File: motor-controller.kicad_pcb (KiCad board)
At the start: 2 copper layers, 40 x 40 mm, 34 parts, among them J1 GH1.25, J2 GH1.25, J3 GH1.25, J4 SM03B-PASS, U1 SSP7903P33PR, U2 AS5600, U3 SS6343M, U4 STM32F031C6T6, Y1 YSX530GA 8MHz

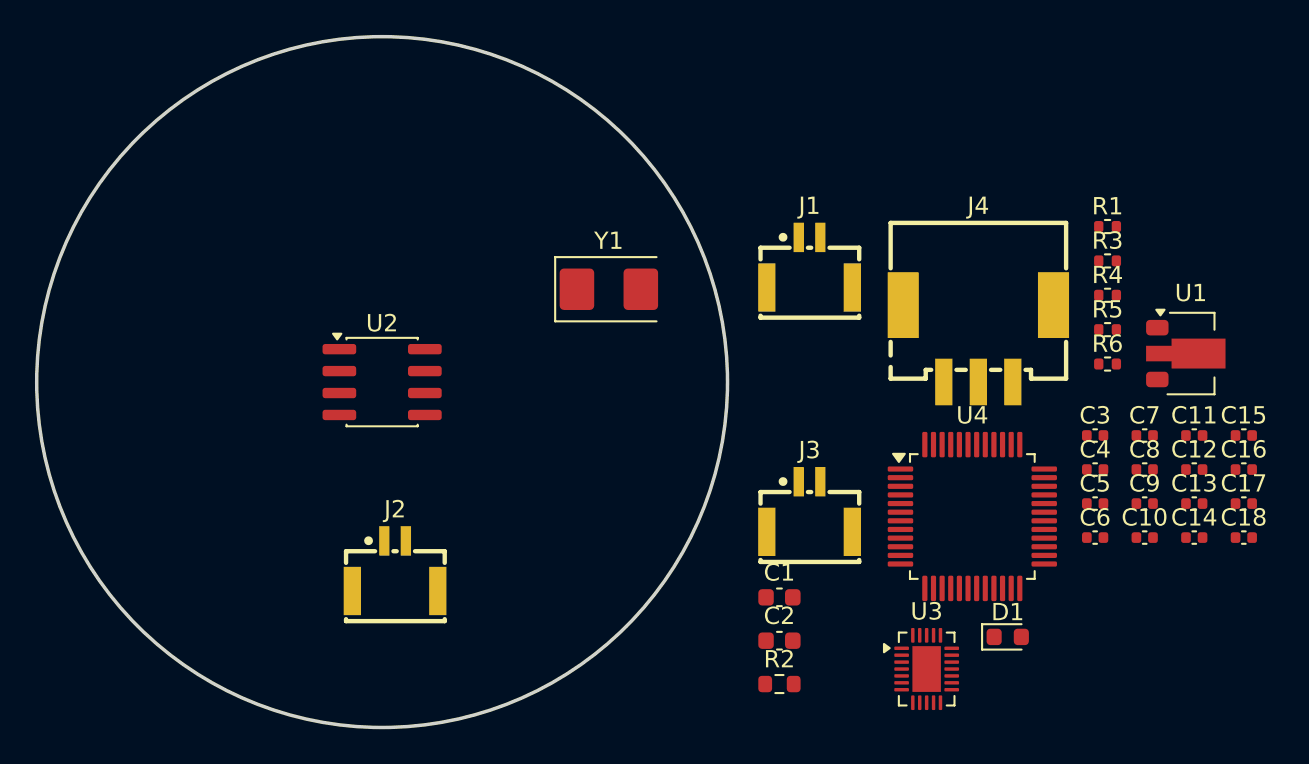
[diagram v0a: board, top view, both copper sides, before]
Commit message: 完成PCB布局
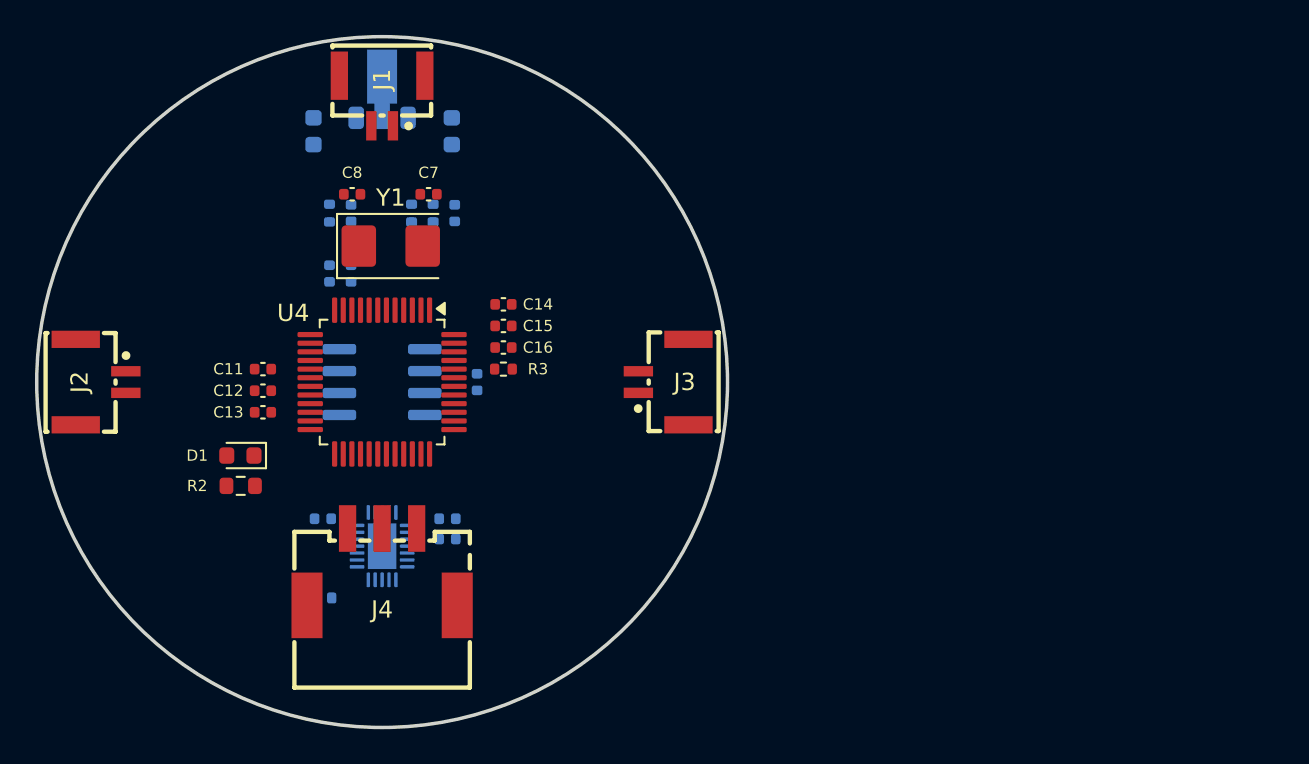
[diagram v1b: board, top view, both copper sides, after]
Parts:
- C1, C10, C17, C18, C2, C3, C4, C5, C6, C9, R1, R4, R5, R6, U1, U2, U3: moved to B.Cu
- moved C17 54.6 mm to (147.0, 91.7), turned to 90 degrees
- moved C13 54.2 mm to (143.1, 99.8)
- moved C12 54.1 mm to (143.1, 98.5)
- moved C11 54.1 mm to (143.1, 97.2)
- moved C18 53.9 mm to (148.2, 91.7), turned to 90 degrees
- moved R1 50.3 mm to (146.6, 110.5), turned to 180 degrees
- moved U1 49.4 mm to (150.0, 80.8), turned to 90 degrees
- moved C9 48.9 mm to (148.2, 88.2), turned to 90 degrees
- moved C8 48.6 mm to (148.3, 87.1), turned to 180 degrees
- moved D1 45.7 mm to (141.8, 102.3), turned to 180 degrees
- moved R4 45.3 mm to (147.0, 88.2), turned to -90 degrees
- moved C6 44.7 mm to (146.6, 105.9), turned to 180 degrees
- moved C10 44.1 mm to (154.2, 88.2), turned to -90 degrees
- moved C7 43.8 mm to (152.7, 87.1)
- moved C16 43.4 mm to (157.0, 96.0)
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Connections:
- J1 pad 1: 12V -> GND
- J1 pad 2: GND -> 12V
- J4 pad 1: /C -> /A
- J4 pad 3: /A -> /C

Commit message: 重新布局并完成布线，添加STM项目定义文件
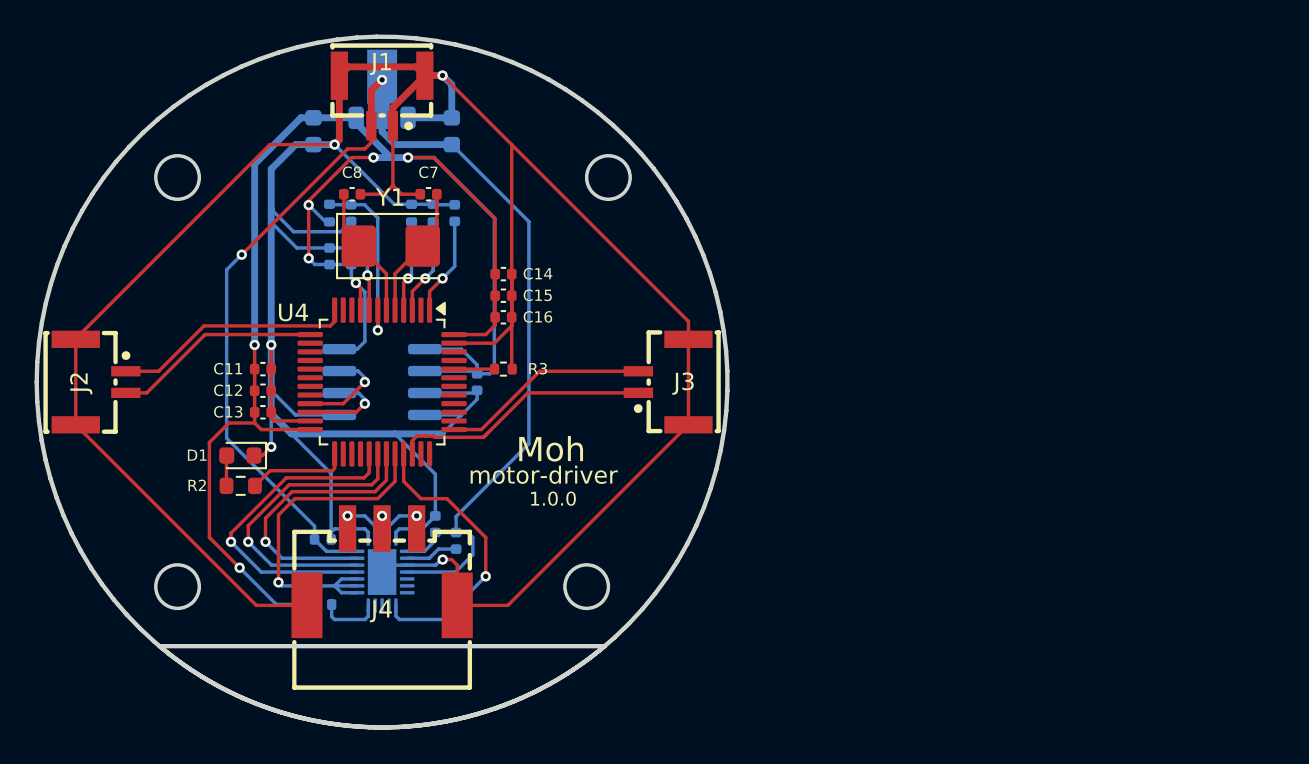
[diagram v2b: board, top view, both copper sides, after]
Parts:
- moved C14 1.75 mm to (157.0, 91.8)
- moved C15 1.75 mm to (157.0, 93.0)
- moved C16 1.75 mm to (157.0, 94.2)
- moved U3 1.50 mm to (150.0, 109.0)
- moved C6 1.19 mm to (146.6, 107.1), turned to 0 degrees
- moved C17 1.00 mm to (147.0, 90.7)
- moved C18 1.00 mm to (148.2, 90.7)
- moved C5 0.77 mm to (153.1, 106.2), turned to 90 degrees
- moved C4 0.51 mm to (154.3, 107.2), turned to 90 degrees
- moved R1 0.38 mm to (146.6, 110.9)
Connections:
- J1 pad 3: (no net) -> GND
- J1 pad 4: (no net) -> GND
- J2 pad 3: (no net) -> GND
- J2 pad 4: (no net) -> GND
- J3 pad 3: (no net) -> GND
- J3 pad 4: (no net) -> GND
- J4 pad 4: (no net) -> GND
- J4 pad 5: (no net) -> GND
- U4 pad 12: unconnected-(U4-PA2-Pad12) -> /Tx
- U4 pad 26: /FAULT -> unconnected-(U4-PB13-Pad26)
- U4 pad 33: unconnected-(U4-PA12-Pad33) -> /FAULT
- U4 pad 42: /Tx -> unconnected-(U4-PB6-Pad42)
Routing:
- net GND: track 0.00 -> 233.7 mm, vias 0 -> 6
- net 3.3V: track 0.00 -> 105.9 mm, vias 0 -> 7
- net 12V: track 0.00 -> 76.9 mm, vias 0 -> 2
- net /EN: track 0.00 -> 20.6 mm, vias 0 -> 1
- net /PWMA: track 0.00 -> 19.1 mm, vias 0 -> 1
- net /PWMB: track 0.00 -> 17.9 mm, vias 0 -> 1
- net /FAULT: track 0.00 -> 16.9 mm, vias 0 -> 1
- net /PWMC: track 0.00 -> 16.5 mm, vias 0 -> 1
- net /SWDIO: track 0.00 -> 15.5 mm
- net /Tx: track 0.00 -> 13.9 mm
- net /SWCLK: track 0.00 -> 12.1 mm
- net /Rx: track 0.00 -> 12.1 mm
- net /RST: track 0.00 -> 10.8 mm, vias 0 -> 1
- net /X1: track 0.00 -> 7.73 mm
- net /X0: track 0.00 -> 7.71 mm
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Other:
- outline, holes or cut-outs redrawn
- board text added: "1.0.0"
- board text added: "Moh"
- board text added: "motor-driver"

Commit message: 将板框从圆环多边形修改为圆弧和直线组合，避免gerber文件混淆
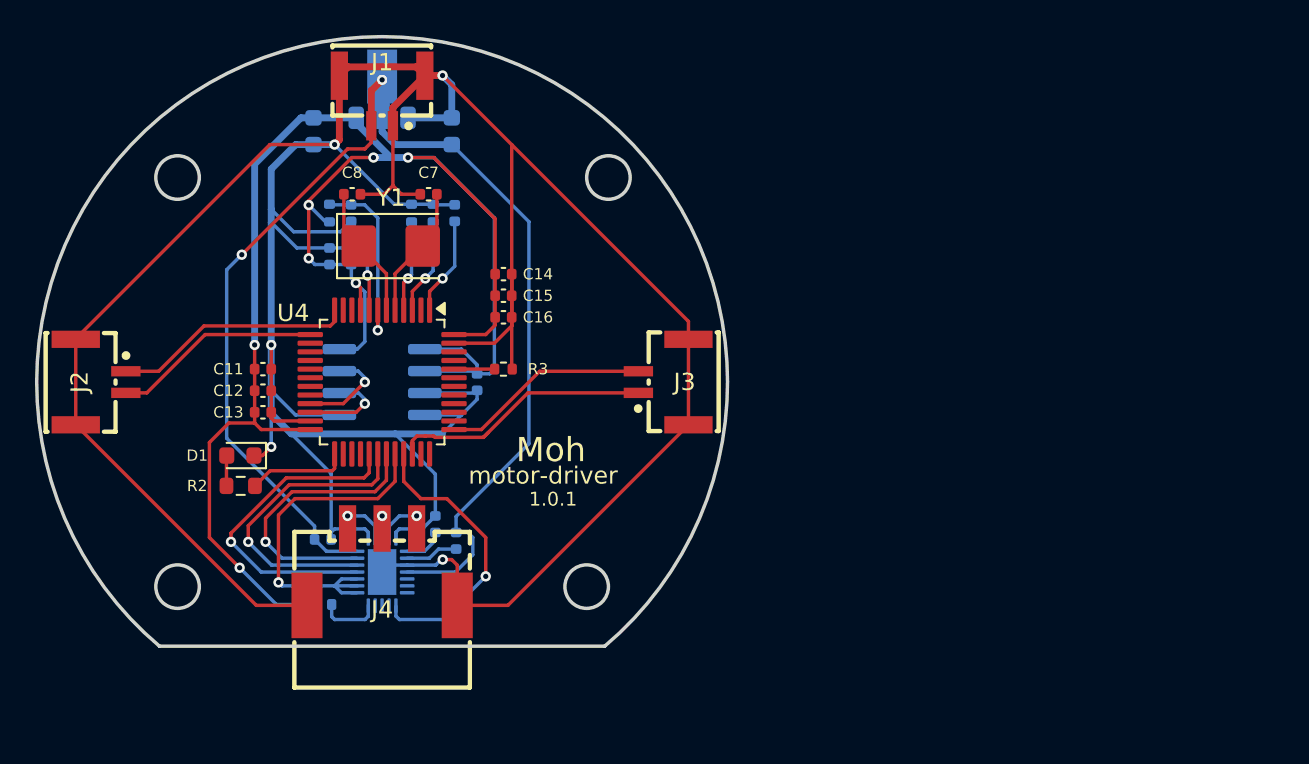
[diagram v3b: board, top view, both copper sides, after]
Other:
- board size 40 x 40 mm -> 40 x 35.3 mm
- board text added: "1.0.1"
- board text removed: "1.0.0"
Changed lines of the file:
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@@
 		(layer "Edge.Cuts")
 	)
-	(gr_poly
-		(pts
-			(arc
-				(start 130 98)
-				(mid 141.567837 116.135937)
-				(end 162.890107 113.292651)
-			)
-			(arc
-				(start 137.109893 113.292651)
-				(mid 168.136478 89.568579)
-				(end 130 98)
-			)
-		)
+	(gr_arc
+		(start 137.109893 113.292651)
+		(mid 150 77.999499)
+		(end 162.890107 113.292651)
 		(stroke
-			(width 0.25)
+			(width 0.2)
 			(type solid)
 		)
-		(fill no)
 		(layer "Edge.Cuts")
 	)
@@
 		(layer "Edge.Cuts")
 	)
-	(gr_text "1.0.0"
+	(gr_line
+		(start 137.109893 113.292651)
+		(end 162.890107 113.292651)
+		(stroke
+			(width 0.2)
+			(type solid)
+		)
+		(layer "Edge.Cuts")
+	)
+	(gr_text "1.0.1"
 		(at 158.5 105.25 0)
 		(layer "F.SilkS")

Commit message: 修正机械安装孔位，修整布线
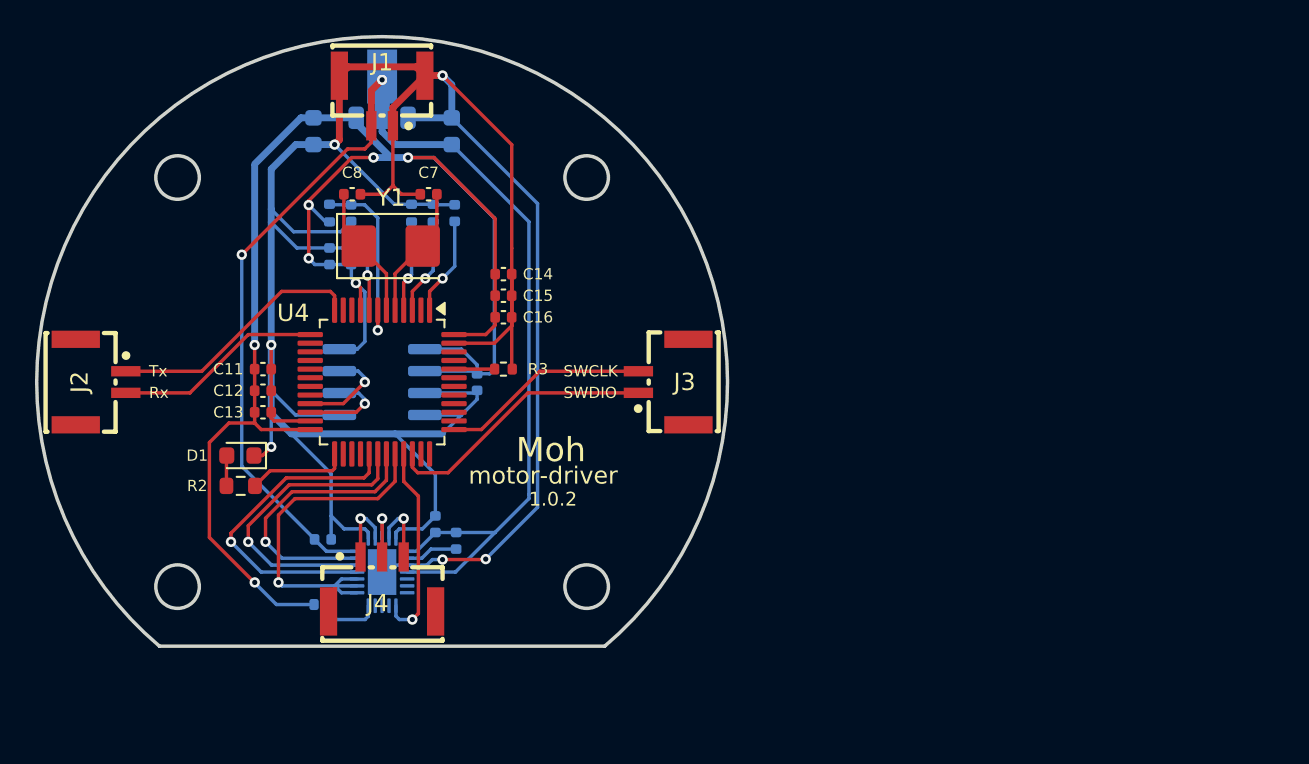
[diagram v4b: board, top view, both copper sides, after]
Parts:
- J4: value SM03B-PASS -> GH1.25; footprint LCEDA_Connector_JST:CONN-SMD_SM03B-PASS-TBT -> LCEDA_Connector_Wafer:CONN-TH_3P-P1.25_GH1.25-WAFER-GH1.25-3PWB
- moved J4 1.00 mm to (150.0, 109.7), turned to 0 degrees
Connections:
- J2 pad 3: GND -> unconnected-(J2-Pin_3-Pad3)
- J2 pad 4: GND -> unconnected-(J2-Pin_4-Pad4)
- J3 pad 3: GND -> unconnected-(J3-Pin_3-Pad3)
- J3 pad 4: GND -> unconnected-(J3-Pin_4-Pad4)
- J4 pad 4: GND -> unconnected-(J4-Pin_4-Pad4)
- J4 pad 5: GND -> unconnected-(J4-Pin_5-Pad5)
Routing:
- net GND: track 233.7 -> 181.1 mm, vias 6 -> 7
- net /FAULT: track 16.9 -> 11.7 mm
- net /B: track 1.30 -> 3.40 mm
- net /C: track 2.55 -> 3.92 mm
- net /A: track 2.55 -> 3.92 mm
- net /Tx: track 13.9 -> 14.9 mm
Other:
- outline, holes or cut-outs redrawn
- board text added: "1.0.2"
- board text added: "M2.5x4"
- board text added: "Rx"
- board text added: "SWCLK"
- board text added: "SWDIO"
- board text added: "Tx"
- board text removed: "1.0.1"
